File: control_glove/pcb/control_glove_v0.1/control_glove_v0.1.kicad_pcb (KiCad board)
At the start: 2 copper layers, 194 x 51 mm, 47 parts, among them J1 Conn_01x04_Female, J2 Conn_01x04_Female, J3 Conn_01x03_Female, J4 Conn_01x03_Female, J5 Conn_01x03_Female, J6 Conn_01x03_Female, J7 Conn_01x04_Female, J8 Conn_01x04_Female, P1 Power_Pins, Q1 Q_NPN_ECB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

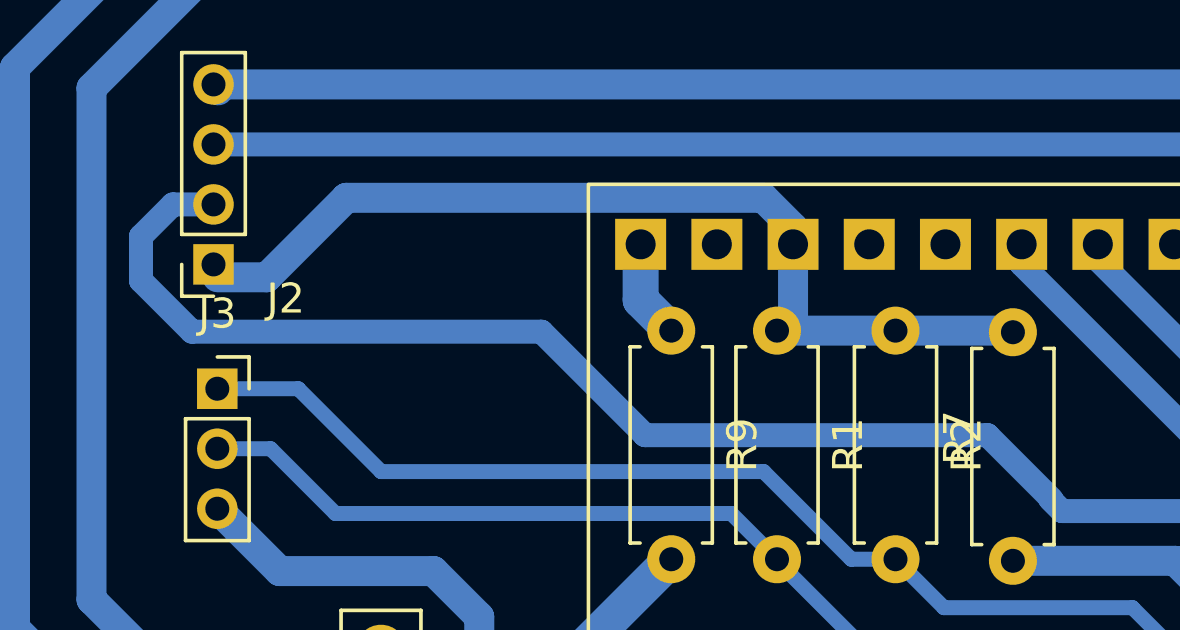
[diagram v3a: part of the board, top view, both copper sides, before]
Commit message: update: Test Control Glove v0.1 PCB success
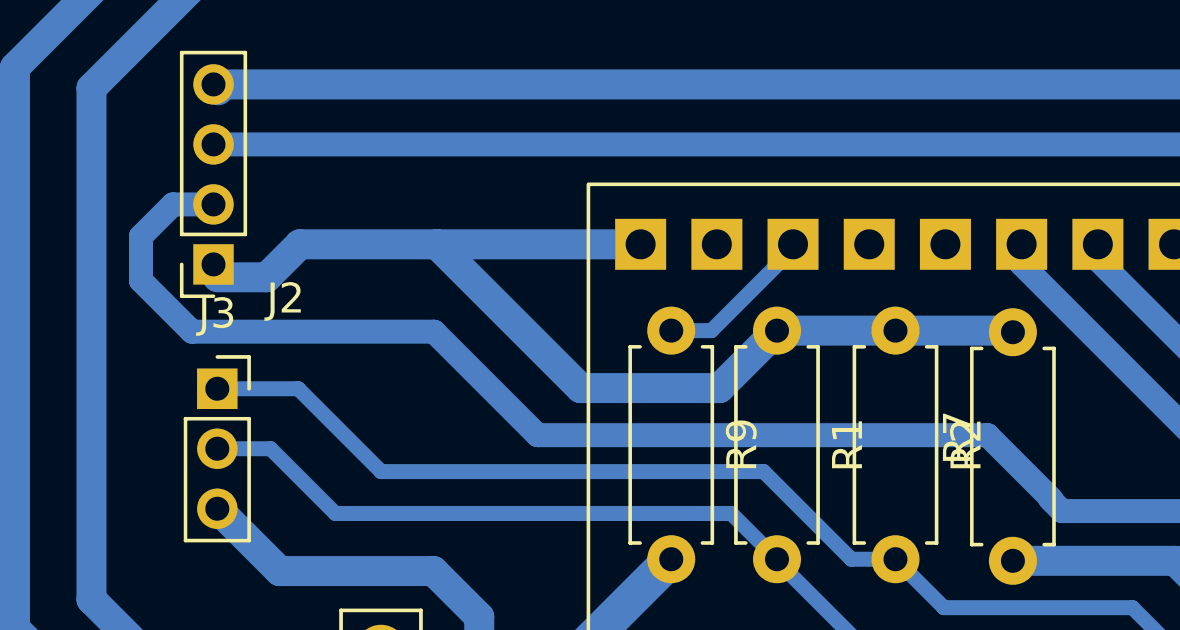
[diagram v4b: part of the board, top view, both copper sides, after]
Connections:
- MCU1 pad 18: 3.3V -> 5V
- MCU1 pad 20: 5V -> 3.3V
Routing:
- net 3.3V: track 32.4 -> 36.8 mm
- net 5V: track 3.30 -> 5.34 mm
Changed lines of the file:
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@@
   (net 71 "Net-(R14-Pad2)")
   (net 72 "Net-(R11-Pad1)")
-  (net 73 "Net-(Q1-Pad2)")
+  (net 73 "Net-(JP1-Pad3)")
   (net 74 "Net-(R13-Pad2)")
   (footprint "Connector_PinHeader_2.54mm:PinHeader_1x08_P2.54mm_Vertical" (layer "F.Cu")
@@
       (net 2 "GND") (pinfunction "E") (pintype "passive"))
     (pad "2" thru_hole oval (at 1.27 0 180) (size 1.05 1.5) (drill 0.75) (layers *.Cu *.Mask)
-      (net 73 "Net-(Q1-Pad2)") (pinfunction "C") (pintype "passive"))
+      (net 73 "Net-(JP1-Pad3)") (pinfunction "C") (pintype "passive"))
     (pad "3" thru_hole oval (at 2.54 0 180) (size 1.05 1.5) (drill 0.75) (layers *.Cu *.Mask)
       (net 11 "Net-(Q1-Pad3)") (pinfunction "B") (pintype "passive"))
@@
       (net 69 "Net-(JP1-Pad2)") (pinfunction "C") (pintype "passive"))
     (pad "3" thru_hole oval (at 0 5.08 270) (size 1.7 1.7) (drill 1) (layers *.Cu *.Mask)
-      (net 73 "Net-(Q1-Pad2)") (pinfunction "B") (pintype "passive"))
+      (net 73 "Net-(JP1-Pad3)") (pinfunction "B") (pintype "passive"))
     (model "${KICAD6_3DMODEL_DIR}/Connector_PinHeader_2.54mm.3dshapes/PinHeader_1x03_P2.54mm_Vertical.wrl"
       (offset (xyz 0 0 0))
@@
       (net 30 "unconnected-(MCU1-Pad17)") (pinfunction "B9") (pintype "bidirectional+no_connect"))
     (pad "18" thru_hole rect (at 0 43.18 270) (size 1.7 1.7) (drill 1) (layers *.Cu *.Mask)
-      (net 5 "3.3V") (pinfunction "3.3V") (pintype "power_out"))
+      (net 32 "5V") (pinfunction "5V") (pintype "power_out"))
     (pad "19" thru_hole rect (at 0 45.72 270) (size 1.7 1.7) (drill 1) (layers *.Cu *.Mask)
       (net 31 "unconnected-(MCU1-Pad19)") (pinfunction "GND") (pintype "bidirectional+no_connect"))
     (pad "20" thru_hole rect (at 0 48.26 270) (size 1.7 1.7) (drill 1) (layers *.Cu *.Mask)
-      (net 32 "5V") (pinfunction "5V") (pintype "power_out"))
+      (net 5 "3.3V") (pinfunction "3.3V") (pintype "power_out"))
     (pad "21" thru_hole rect (at 15 -0.1 270) (size 1.7 1.7) (drill 1) (layers *.Cu *.Mask)
       (net 33 "Net-(MCU1-Pad21)") (pinfunction "5V") (pintype "power_in"))
@@
   (segment (start 28.194 34.322) (end 30.893 34.322) (width 0.5) (layer "B.Cu") (net 4))
   (segment (start 60.18469 43.10469) (end 60.18469 44.508049) (width 0.5) (layer "B.Cu") (net 4))
-  (segment (start 32.493951 27.958049) (end 46.39469 27.958049) (width 1) (layer "B.Cu") (net 5))
+  (segment (start 35.508049 29.508049) (end 30.943951 29.508049) (width 1) (layer "B.Cu") (net 5))
+  (segment (start 44.935 34.3) (end 40.3 34.3) (width 1) (layer "B.Cu") (net 5))
+  (segment (start 46.85 32.385) (end 44.935 34.3) (width 1) (layer "B.Cu") (net 5))
   (segment (start 46.85 32.385) (end 50.8 32.385) (width 1) (layer "B.Cu") (net 5))
-  (segment (start 28.2 30.607) (end 29.845 30.607) (width 1) (layer "B.Cu") (net 5))
-  (segment (start 47.38469 29.508049) (end 47.38469 31.85031) (width 1) (layer "B.Cu") (net 5))
-  (segment (start 46.39469 27.958049) (end 47.38469 28.948049) (width 1) (layer "B.Cu") (net 5))
+  (segment (start 30.943951 29.508049) (end 29.845 30.607) (width 1) (layer "B.Cu") (net 5))
+  (segment (start 40.3 34.3) (end 35.508049 29.508049) (width 1) (layer "B.Cu") (net 5))
+  (segment (start 29.845 30.607) (end 28.2 30.607) (width 1) (layer "B.Cu") (net 5))
   (segment (start 54.661 32.385) (end 54.714 32.438) (width 1) (layer "B.Cu") (net 5))
   (segment (start 46.85 32.385) (end 47 32.235) (width 1.2) (layer "B.Cu") (net 5))
-  (segment (start 47.38469 31.85031) (end 46.85 32.385) (width 1) (layer "B.Cu") (net 5))
-  (segment (start 47.38469 28.948049) (end 47.38469 29.508049) (width 1) (layer "B.Cu") (net 5))
+  (segment (start 42.30469 29.508049) (end 35.508049 29.508049) (width 1) (layer "B.Cu") (net 5))
   (segment (start 50.8 32.385) (end 54.661 32.385) (width 1) (layer "B.Cu") (net 5))
-  (segment (start 29.845 30.607) (end 32.493951 27.958049) (width 1) (layer "B.Cu") (net 5))
   (segment (start 68.08469 41.178049) (end 70.007049 41.178049) (width 0.5) (layer "B.Cu") (net 6))
   (segment (start 71.755 42.926) (end 74.93 42.926) (width 0.5) (layer "B.Cu") (net 6))
@@
   (segment (start 115.38 34) (end 112.89 31.51) (width 0.8) (layer "B.Cu") (net 28))
   (segment (start 103.87 31.51) (end 98.48 36.9) (width 0.8) (layer "B.Cu") (net 28))
-  (segment (start 42.30469 31.36469) (end 43.325 32.385) (width 1.2) (layer "B.Cu") (net 32))
-  (segment (start 42.30469 29.508049) (end 42.30469 31.36469) (width 1.2) (layer "B.Cu") (net 32))
+  (segment (start 47.38469 29.66531) (end 44.665 32.385) (width 0.5) (layer "B.Cu") (net 32))
+  (segment (start 47.38469 29.508049) (end 47.38469 29.66531) (width 0.5) (layer "B.Cu") (net 32))
+  (segment (start 44.665 32.385) (end 43.325 32.385) (width 0.5) (layer "B.Cu") (net 32))
   (segment (start 103.39469 52.178049) (end 103.39469 43.70469) (width 1.2) (layer "B.Cu") (net 33))
   (segment (start 91.522739 43.65) (end 90.66469 44.508049) (width 1.2) (layer "B.Cu") (net 33))
@@
   (segment (start 108.331 45.593) (end 108.424 45.5) (width 1.2) (layer "B.Cu") (net 34))
   (segment (start 108.424 45.5) (end 116.75 45.5) (width 1.2) (layer "B.Cu") (net 34))
+  (segment (start 27.35 32.42) (end 35.42 32.42) (width 0.8) (layer "B.Cu") (net 35))
   (segment (start 83.04469 43.32469) (end 83.04469 44.508049) (width 0.8) (layer "B.Cu") (net 35))
-  (segment (start 42.45 35.87) (end 53.87 35.87) (width 0.8) (layer "B.Cu") (net 35))
-  (segment (start 27.35 32.42) (end 39 32.42) (width 0.8) (layer "B.Cu") (net 35))
-  (segment (start 53.87 35.87) (end 56 38) (width 0.8) (layer "B.Cu") (net 35))
+  (segment (start 26.712 28.178) (end 25.65 29.24) (width 0.8) (layer "B.Cu") (net 35))
   (segment (start 25.65 29.24) (end 25.65 30.72) (width 0.8) (layer "B.Cu") (net 35))
   (segment (start 55.951899 38) (end 56.351899 38.4) (width 0.8) (layer "B.Cu") (net 35))
-  (segment (start 39 32.42) (end 42.45 35.87) (width 0.8) (layer "B.Cu") (net 35))
-  (segment (start 26.712 28.178) (end 25.65 29.24) (width 0.8) (layer "B.Cu") (net 35))
+  (segment (start 56.351899 38.4) (end 78.12 38.4) (width 0.8) (layer "B.Cu") (net 35))
+  (segment (start 35.42 32.42) (end 38.87 35.87) (width 0.8) (layer "B.Cu") (net 35))
+  (segment (start 53.87 35.87) (end 56 38) (width 0.8) (layer "B.Cu") (net 35))
+  (segment (start 78.12 38.4) (end 83.04469 43.32469) (width 0.8) (layer "B.Cu") (net 35))
   (segment (start 25.65 30.72) (end 27.35 32.42) (width 0.8) (layer "B.Cu") (net 35))
-  (segment (start 56.351899 38.4) (end 78.12 38.4) (width 0.8) (layer "B.Cu") (net 35))
+  (segment (start 38.87 35.87) (end 53.87 35.87) (width 0.8) (layer "B.Cu") (net 35))
   (segment (start 28.067 28.178) (end 26.712 28.178) (width 0.8) (layer "B.Cu") (net 35))
-  (segment (start 78.12 38.4) (end 83.04469 43.32469) (width 0.8) (layer "B.Cu") (net 35))
   (segment (start 58.673 48) (end 55.753 50.92) (width 0.5) (layer "B.Cu") (net 36))
   (segment (start 64 48) (end 58.673 48) (width 0.5) (layer "B.Cu") (net 36))

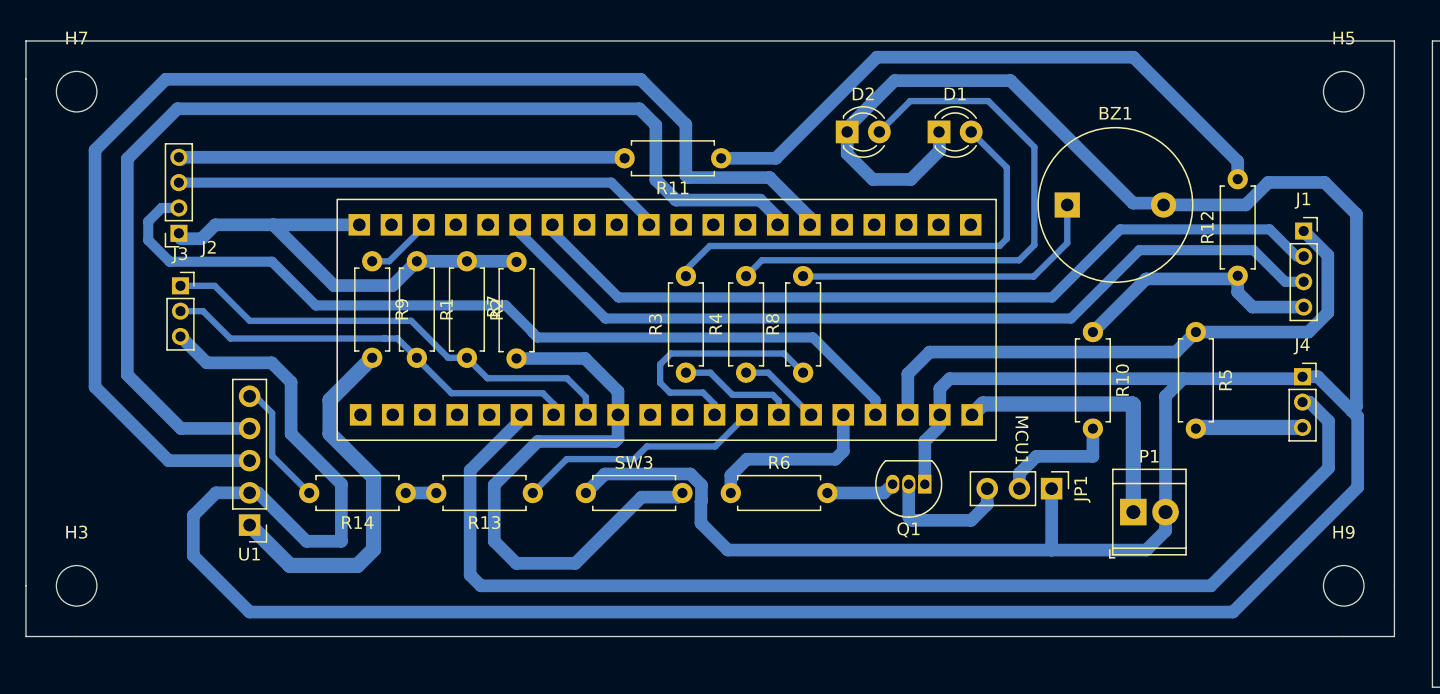
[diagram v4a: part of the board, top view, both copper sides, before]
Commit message: update: Add switch and trigger button and remove unused components
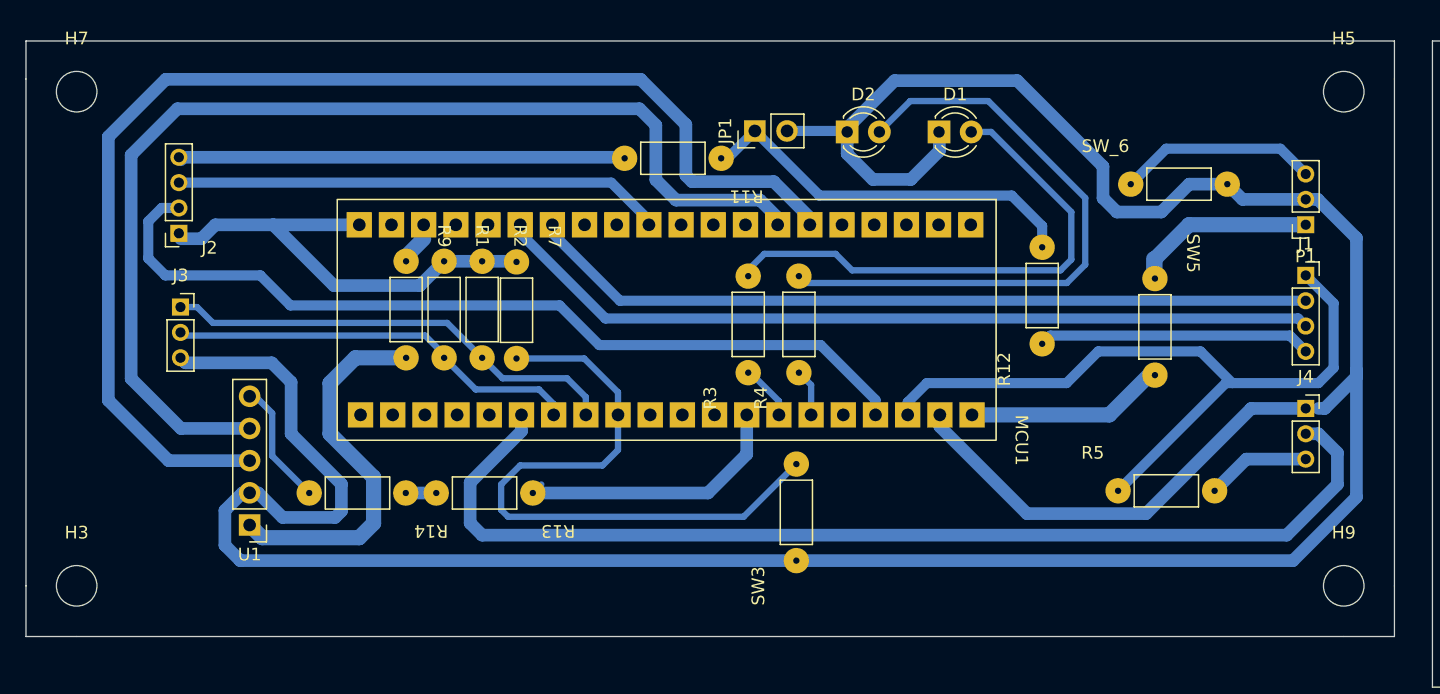
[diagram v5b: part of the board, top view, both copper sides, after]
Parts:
- removed BZ1: Buzzer, Buzzer_Beeper:Buzzer_12x9.5RM7.6
- removed Q1: Q_NPN_ECB, Package_TO_SOT_THT:TO-92_Inline
- removed R10: 0, Resistor_THT:R_Axial_DIN0207_L6.3mm_D2.5mm_P7.62mm_Horizontal
- removed R6, R8: 300, Resistor_THT:R_Axial_DIN0207_L6.3mm_D2.5mm_P7.62mm_Horizontal
- added SW5: SW_DIP_x01, hieu:resistor, F.Cu at (105.1, 33.8)
- added SW_6: SW_Push, hieu:resistor, F.Cu at (103.2, 26.3)
- JP1: value Jumper_3_Bridged12 -> Jumper_2_Bridged; footprint Connector_PinHeader_2.54mm:PinHeader_1x03_P2.54mm_Vertical -> Connector_PinHeader_2.54mm:PinHeader_1x02_P2.54mm_Vertical
- P1: footprint TerminalBlock_TE-Connectivity:TerminalBlock_TE_282834-2_1x02_P2.54mm_Horizontal -> Connector_PinSocket_2.00mm:PinSocket_1x03_P2.00mm_Vertical
- R1, R11, R12, R13, R14, R2, R3, R4, R5, R7, R9, SW3: footprint Resistor_THT:R_Axial_DIN0207_L6.3mm_D2.5mm_P7.62mm_Horizontal -> hieu:resistor
- moved JP1 36.7 mm to (73.5, 22.1), turned to 90 degrees
- moved P1 26.4 mm to (117.0, 29.5), turned to 180 degrees
- moved SW3 17.4 mm to (76.8, 56.0), turned to 90 degrees
- moved R12 16.3 mm to (96.2, 38.9)
- moved R5 14.0 mm to (102.2, 50.5), turned to 0 degrees
- moved R3 4.92 mm to (73.0, 41.2)
- moved R4 4.17 mm to (77.0, 41.2)
- moved J1 3.50 mm to (117.0, 33.5)
- moved R9 2.67 mm to (46.0, 32.4)
- moved J4 2.51 mm to (117.0, 44.0)
- moved R1 2.15 mm to (49.0, 32.4)
- moved J3 1.68 mm to (28.2, 36.0)
- moved R2 1.20 mm to (52.0, 32.4)
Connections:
- JP1 pad 1: GND -> Net-(R12-Pad2)
- JP1 pad 2: Net-(JP1-Pad2) -> GND
- MCU1 pad 25: SENSOR-PWR-EN -> unconnected-(MCU1-Pad25)
- MCU1 pad 29: BUZZER -> unconnected-(MCU1-Pad29)
- P1 pad 1: Net-(MCU1-Pad21) -> Net-(P1-Pad1)
- R11 pad 1: Net-(R11-Pad1) -> Net-(R12-Pad2)
- R12 pad 2: Net-(R11-Pad1) -> Net-(R12-Pad2)
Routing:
- net GND: track 331.5 -> 256.2 mm
- net Net-(R11-Pad1): track 48.9 -> 0.00 mm
- net Net-(R12-Pad2): track 0.00 -> 31.0 mm
- net Net-(BZ1-Pad1): track 25.4 -> 0.00 mm
- net BUZZER: track 19.6 -> 0.00 mm
- net Net-(P1-Pad1): track 0.00 -> 16.2 mm
- net Net-(P1-Pad3): track 0.00 -> 15.8 mm
- net SENSOR-PWR-EN: track 14.4 -> 0.00 mm
- net 3.3V-SHOULDER: track 44.7 -> 58.7 mm
- net Net-(JP1-Pad3): track 10.7 -> 0.00 mm
- net Net-(JP1-Pad2): track 9.75 -> 0.00 mm
- net RV1: track 92.6 -> 86.3 mm
- net Net-(Q1-Pad3): track 5.44 -> 0.00 mm
- net Net-(MCU1-Pad21): track 21.6 -> 16.2 mm
- net Net-(D1-Pad2): track 35.9 -> 41.2 mm
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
